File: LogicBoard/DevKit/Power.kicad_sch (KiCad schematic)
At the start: 17 parts, among them J23 DriverVoltageSelect, U14 REF3033AIDBZR, U16 TPS5430DDAR, U9 AMS1117-3.3

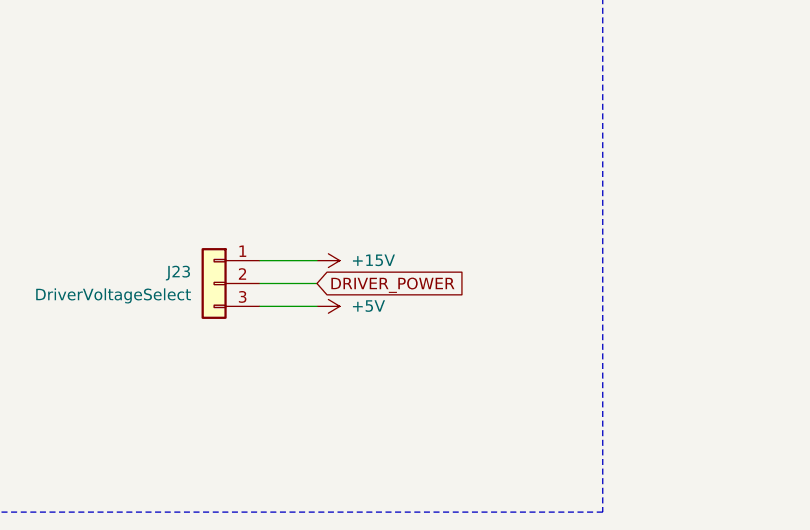
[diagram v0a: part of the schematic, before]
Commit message: v3.3.2 - ECP2304 changes
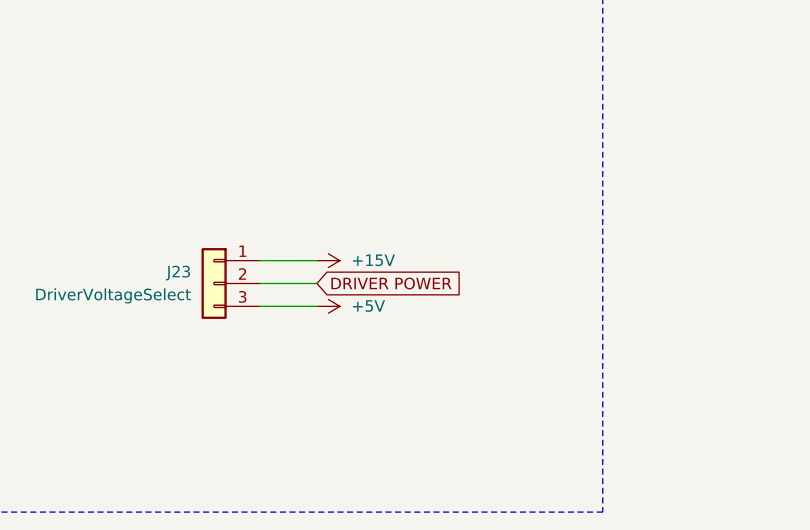
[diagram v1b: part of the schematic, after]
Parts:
- U14, U9: JLCRotOffset -180 -> 0
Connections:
- net DRIVER_POWER renamed DRIVER POWER
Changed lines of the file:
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@@
 		)
 	)
-	(global_label "DRIVER_POWER"
+	(global_label "DRIVER POWER"
 		(shape input)
 		(at 158.75 139.7 0)
@@
 			)
 		)
-		(property "JLCRotOffset" "-180"
+		(property "JLCRotOffset" "0"
 			(at 196.85 57.15 0)
 			(effects
@@
 			)
 		)
-		(property "JLCRotOffset" "-180"
+		(property "JLCRotOffset" "0"
 			(at 63.5 133.35 0)
 			(effects
